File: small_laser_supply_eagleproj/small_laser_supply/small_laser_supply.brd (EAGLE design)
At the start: 50.8 x 25.4 mm, 7 parts, among them X1 5V_IN, X2 CTRL, X3 OUT

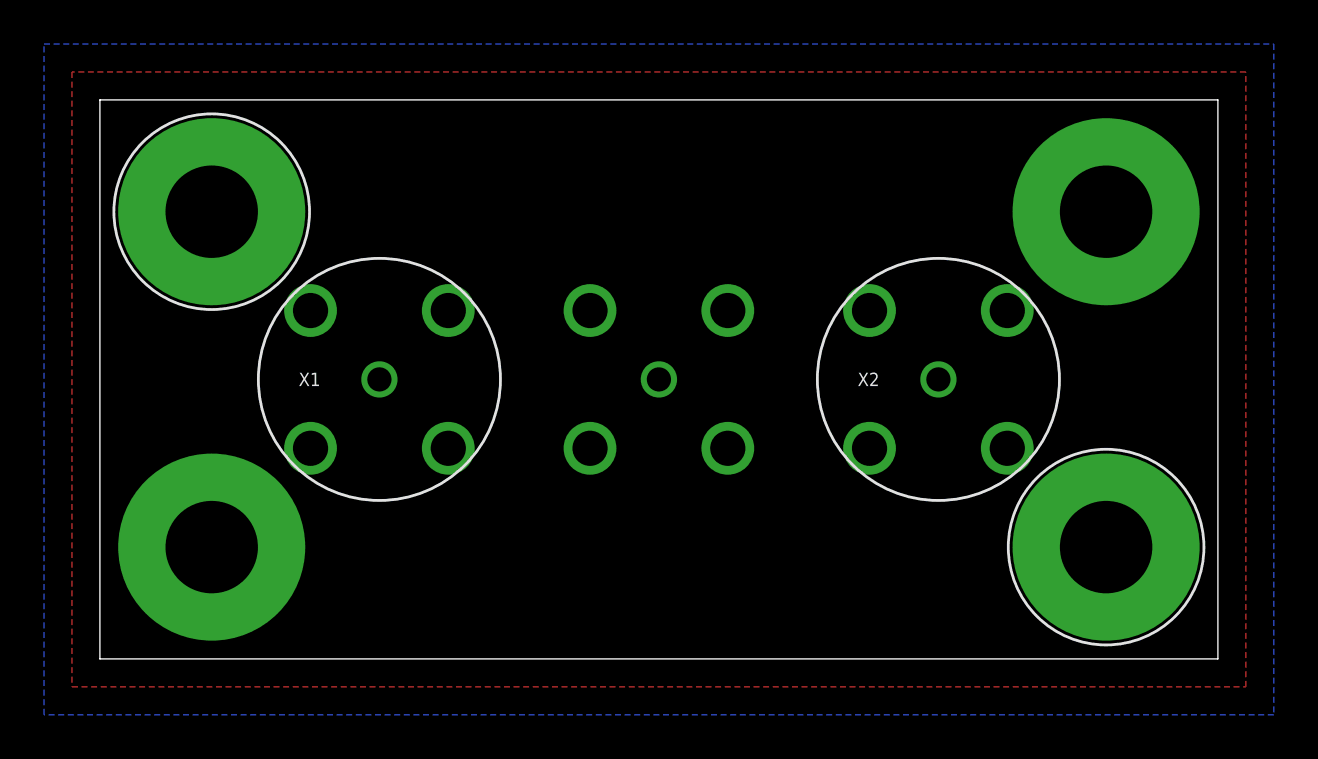
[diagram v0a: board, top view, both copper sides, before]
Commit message: Nearly finished the schematic and initial board layout (before routing traces)
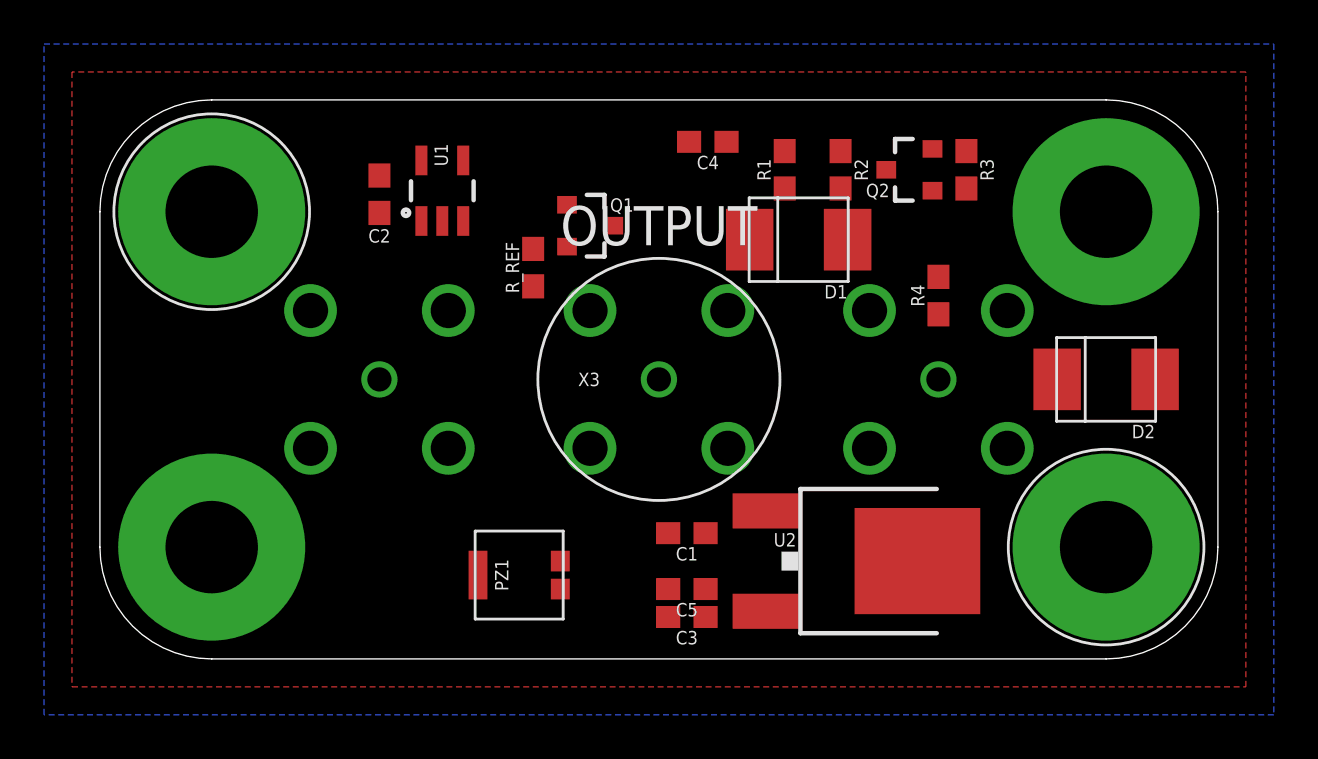
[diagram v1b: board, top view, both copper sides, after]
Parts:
- added C1, C2, C3: .1uF, small_laser_supply_lib:0603
- added C4, C5: 1uF, small_laser_supply_lib:0603
- added D1, D2: 5.5v, small_laser_supply_lib:DO-214AA
- added PZ1: 16v, small_laser_supply_lib:POLYZEN_LS
- added Q1, Q2: (no value), small_laser_supply_lib:SOT23-3
- added R1: 442, small_laser_supply_lib:0603
- added R2: 4020, small_laser_supply_lib:0603
- added R3: 10k, small_laser_supply_lib:0603
- added R4: 100, small_laser_supply_lib:0603
- added R_REF: 165, small_laser_supply_lib:0603
- added U1: LT6003_SOT23-5, small_laser_supply_lib:SOT23-5
- added U2: 5v, small_laser_supply_lib:DPAK
- X1: value 5V_IN -> VIN
- flipped X1 to the bottom
- flipped X2 to the bottom
- flipped X3 to the top
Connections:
- new net 5V: C2.1, C3.1, C5.1, R1.1, R_REF.1, U1.5, U2.3
- new net N$1: Q1.2, R_REF.2, U1.4
- new net N$10: Q1.1, U1.1
- new net N$2: D1.C, Q1.3, X3.C
- new net N$3: C1.1, PZ1.VOUT, U2.1
- new net N$4: Q2.1, R3.1, R4.2
- new net N$5: Q2.3, R2.2
- new net N$6: C4.1, R1.2, R2.1, U1.3
- new net N$7: D2.C, R4.1, X2.C
- new net VIN: PZ1.VIN, X1.C
- net GND: now also C1.2, C2.2, C3.2, C4.2, C5.2, D1.A, D2.A, PZ1.GND, Q2.2, R3.2, U1.2, U2.4
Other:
- outline, holes or cut-outs redrawn
- board text added: "OUTPUT"
- board text added: "TRIG"
- board text added: "V IN"

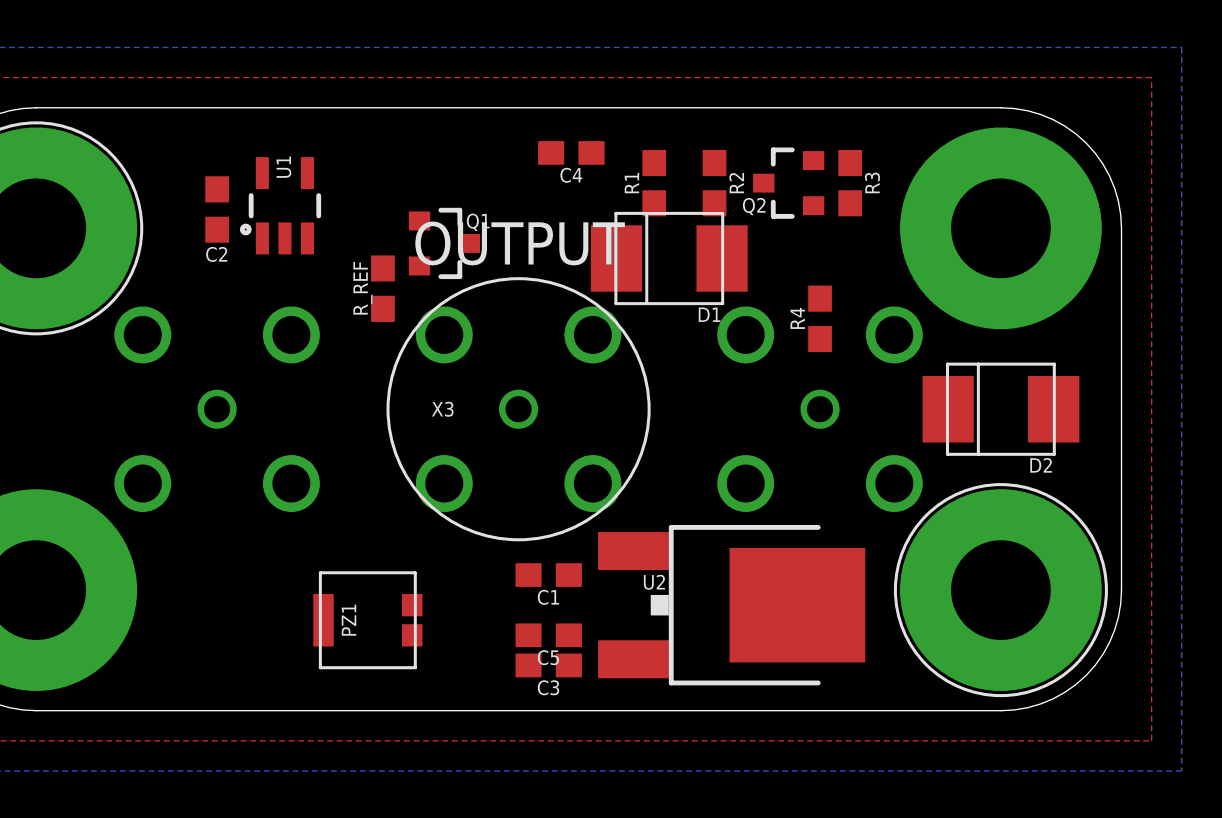
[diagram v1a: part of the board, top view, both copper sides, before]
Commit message: lots more work on the board and schematic before realizing the laser diode is actually backwards and we need to pull current out of ground
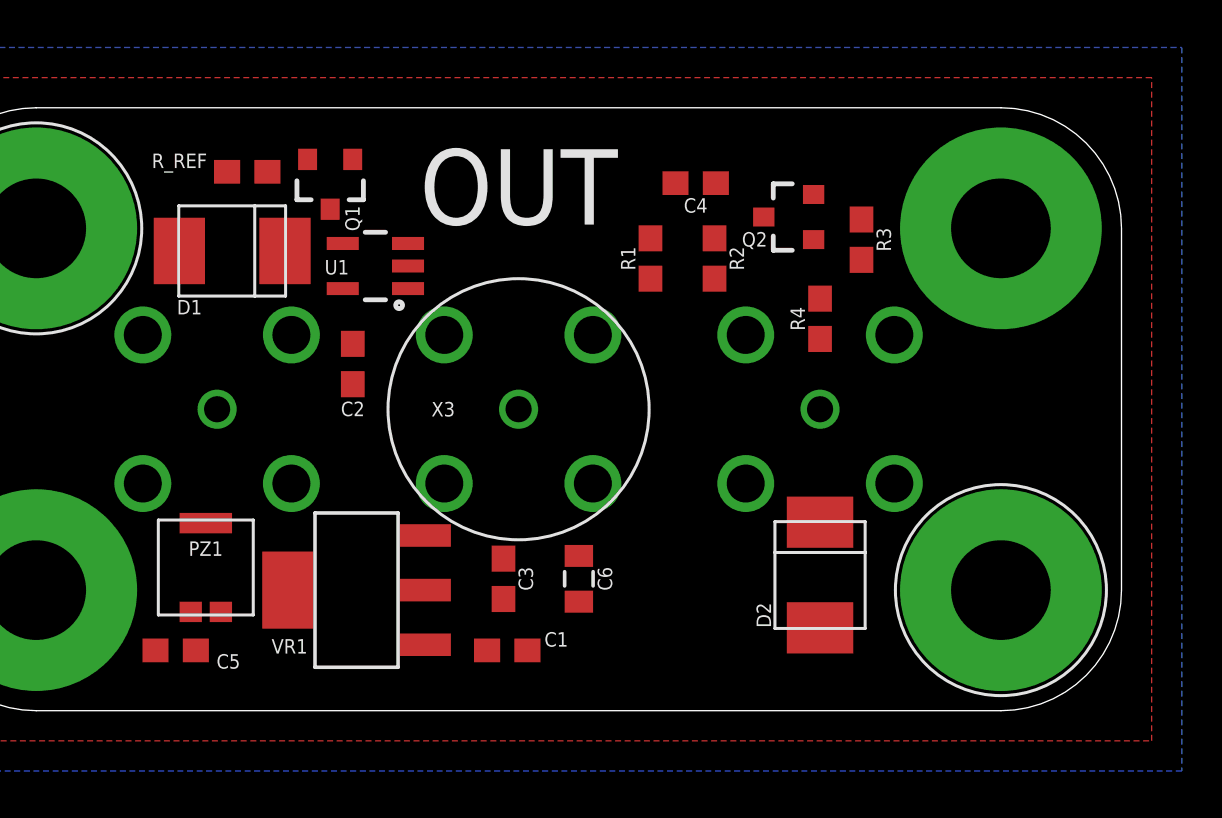
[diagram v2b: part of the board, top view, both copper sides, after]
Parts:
- removed U2: 5v, small_laser_supply_lib:DPAK
- added C6: 22uF, small_laser_supply_lib:0805
- added VR1: (no value), small_laser_supply_lib:SOT-223
- moved D1 18.4 mm to (13.3, 19.4), turned to 0 degrees
- moved C5 15.7 mm to (11.0, 2.54)
- moved D2 10.3 mm to (38.1, 5.71), turned to 90 degrees
- moved C2 8.66 mm to (18.4, 14.6)
- moved R_REF 7.54 mm to (14.0, 22.7), turned to 0 degrees
- moved PZ1 7.18 mm to (12.2, 6.03), turned to 270 degrees
- moved Q1 5.40 mm to (17.5, 22.2), turned to 180 degrees
- moved C4 5.39 mm to (32.9, 22.2)
- moved U1 4.58 mm to (19.4, 18.7), turned to 90 degrees
- moved C3 4.12 mm to (24.8, 5.56), turned to 270 degrees
- moved C1 3.62 mm to (24.9, 2.54), turned to 0 degrees
- moved R1 3.18 mm to (31.0, 19.1)
- moved R2 3.18 mm to (33.7, 19.1)
- moved R3 2.43 mm to (39.8, 19.8)
- moved Q2 1.43 mm to (36.8, 20.8)
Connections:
- net 5V: now also C6.1, VR1.3; no longer C5.1, U2.3
- net GND: now also C6.2, VR1.2, VR1.4; no longer U2.4
- net N$3: now also C5.1, VR1.1; no longer U2.1
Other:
- board text added: "3mA CC"
- board text added: "OUT"
- board text removed: "OUTPUT"

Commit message: Fixed version of the schematic seems to be finished
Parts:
- removed PZ1: 16v, small_laser_supply_lib:POLYZEN_LS
- removed R3: 10k, small_laser_supply_lib:0603
- removed R4: 100, small_laser_supply_lib:0603
- added D3: 18v, small_laser_supply_lib:DO-214AA
- added PTC1: 800mA, small_laser_supply_lib:2SMD_PTC
- C1, C2, C3: value .1uF -> 1uF
- C4, C5: value 1uF -> .1uF
- C6: value 22uF -> .1uF; device small_laser_supply_lib:0805 -> small_laser_supply_lib:0603
- R1: value 442 -> 4020
- R2: value 4020 -> 442
- VR1: value (none) -> -5V; device small_laser_supply_lib:SOT-223 -> small_laser_supply_lib:DPAK
- moved Q2 115.8 mm to (-52.1, -53.3), turned to 0 degrees
- moved C4 100.0 mm to (-39.4, -47.0), turned to 0 degrees
- moved C2 91.6 mm to (-45.7, -50.8), turned to 0 degrees
- moved Q1 81.1 mm to (-40.6, -34.3), turned to 0 degrees
- moved C6 80.9 mm to (-39.4, -39.4), turned to 0 degrees
- moved C5 80.5 mm to (-45.7, -54.6), turned to 0 degrees
- moved C1 78.9 mm to (-39.4, -43.2)
- moved VR1 77.4 mm to (-45.7, -38.1), turned to 0 degrees
- moved C3 18.5 mm to (32.9, 22.2), turned to 180 degrees
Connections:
- removed net 5V: C2.1, C3.1, C6.1, R1.1, R_REF.1, U1.5, VR1.3
- removed net N$1 (its old number): Q1.2, R_REF.2, U1.4
- removed net N$5: Q2.3, R2.2
- removed net VIN: PZ1.VIN, X1.C
- new net -5V: C2.2, C5.2, C6.2, R2.2, R_REF.2, U1.2, VR1.3
- new net N$8: C1.2, C4.2, D3.A, PTC1.2, VR1.4
- new net N$9: D2.A, Q2.1, X2.C
- net GND: now also C1.1, C2.1, C3.1, C4.1, C5.1, C6.1, D1.C, D2.C, D3.C, U1.5, VR1.1; no longer C1.2, C2.2, C3.2, C4.2, C5.2, C6.2, D1.A, D2.A, PZ1.GND, R3.2, U1.2, VR1.2, VR1.4
- net N$2: now also Q1.2, R_REF.1, U1.4; no longer D1.C, Q1.3, X3.C
- net N$3: now also Q2.3, R1.1; no longer C1.1, C5.1, PZ1.VOUT, VR1.1
- net N$4: now also PTC1.1, X1.C; no longer Q2.1, R3.1, R4.2
- net N$6: now also C3.2; no longer C4.1
- net N$7: now also D1.A, Q1.3, X3.C; no longer D2.C, R4.1, X2.C

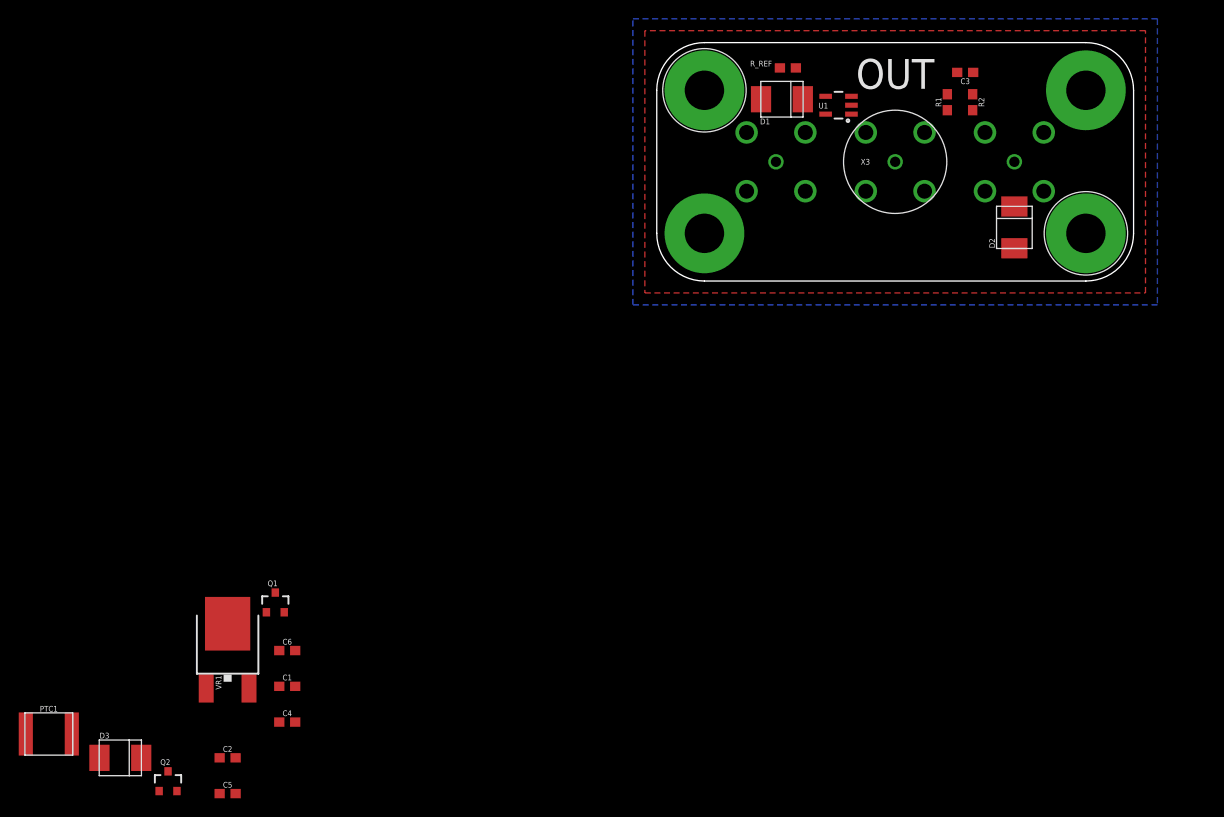
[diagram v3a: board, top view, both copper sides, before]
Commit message: Started and probably finished laying out the board and routing traces, need to generate gerber files next.
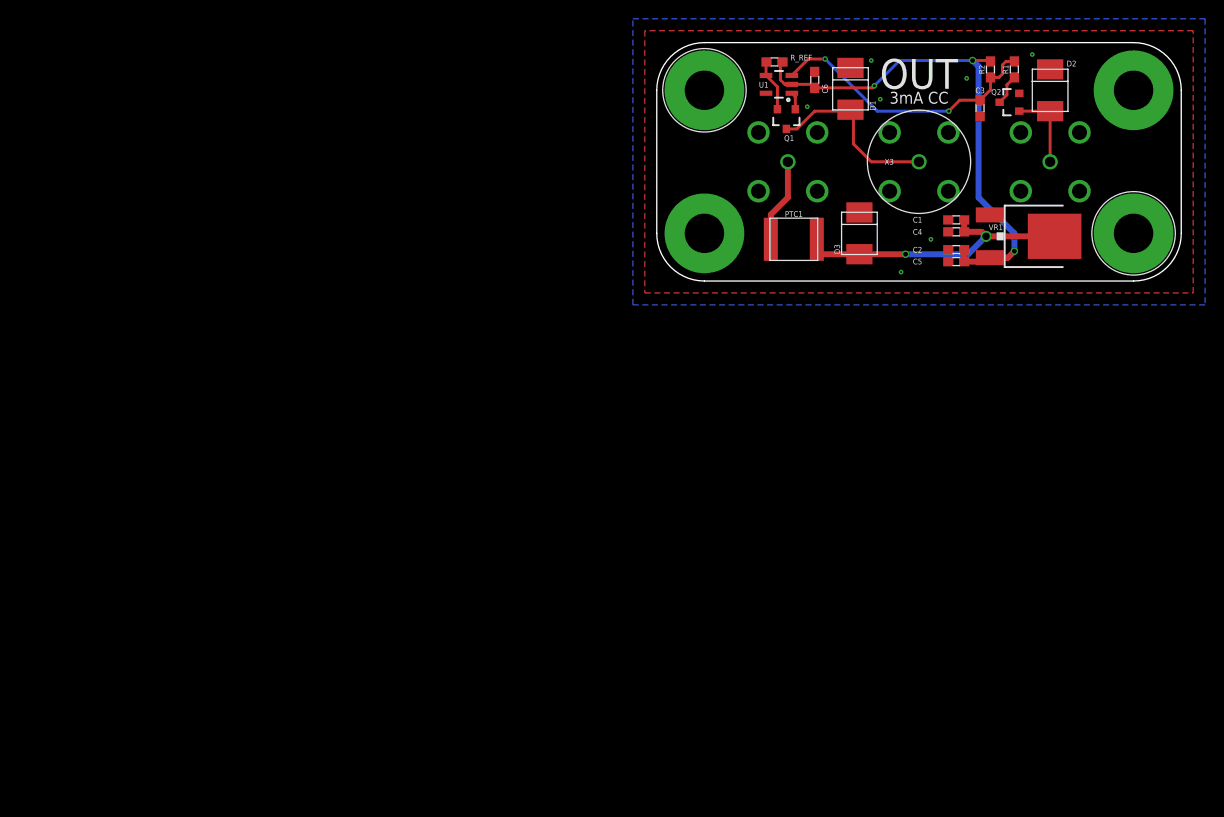
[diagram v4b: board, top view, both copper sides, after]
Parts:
- moved Q2 115.3 mm to (37.6, 19.1), turned to 90 degrees
- moved VR1 96.6 mm to (40.8, 4.76), turned to 270 degrees
- moved D3 96.6 mm to (21.6, 5.08), turned to 90 degrees
- moved C5 96.1 mm to (31.9, 2.06)
- moved PTC1 95.3 mm to (14.6, 4.45)
- moved C2 94.6 mm to (31.9, 3.33)
- moved C4 88.4 mm to (31.9, 5.24)
- moved C1 86.9 mm to (31.9, 6.51)
- moved C6 82.8 mm to (16.8, 21.4), turned to 270 degrees
- moved Q1 75.0 mm to (13.8, 17.3), turned to 180 degrees
- moved D2 15.1 mm to (41.9, 20.3)
- moved R1 7.95 mm to (38.1, 22.5)
- moved D1 7.39 mm to (20.6, 20.5), turned to 90 degrees
- moved U1 6.73 mm to (13.0, 21.0)
- moved MH1 5.08 mm to (50.8, 20.3)
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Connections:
- net N$6 renamed V_REF
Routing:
- net -5V: track 0.00 -> 55.2 mm, vias 0 -> 3
- net N$8: track 0.00 -> 31.3 mm, vias 0 -> 2
- net V_REF: track 0.00 -> 30.3 mm, vias 0 -> 2
- net N$7: track 0.00 -> 19.5 mm
- net N$4: track 0.00 -> 9.01 mm
- net N$9: track 0.00 -> 8.68 mm
- net N$2: track 0.00 -> 5.56 mm
- net N$3: track 0.00 -> 3.30 mm
- net N$1: track 0.00 -> 1.85 mm
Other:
- board size 50.8 x 25.4 mm -> 55.9 x 25.4 mm
- board text added: "-10v to -18v"
- board text added: "-5V:on 0V:off"
- board text added: "Swept Source Laser Driver 3mA CC -5V max Jackson Gray jackmaxg@mit.edu"
